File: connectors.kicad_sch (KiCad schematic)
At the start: 9 parts, among them J1 DX07S024JJ2R1300, J2 PCIe_x4_Conn_EdgeMount

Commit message: Updated libraries, finished PCIe clock generator section
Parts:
- C1, C6: footprint antmicro-footprints:0805-cap -> antmicro-footprints:C_0805_2012Metric
- R1: footprint antmicro-footprints:0402-res -> antmicro-footprints:R_0402_1005Metric
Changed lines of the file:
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@@
     (pin "1")
   )
-  (symbol (lib_name "C_10u_0805_35V_1") (lib_id "antmicroCapacitorsmisc:C_10u_0805_35V") (at 181.61 250.19 90) (unit 1)
+  (symbol (lib_id "antmicroCapacitorsmisc:C_10u_0805_35V") (at 181.61 250.19 90) (unit 1)
     (in_bom yes) (on_board yes)
     (property "Reference" "C6" (id 0) (at 183.515 246.38 90)
@@
       (effects (font (size 1.27 1.27) (thickness 0.15)) (justify left bottom) hide)
     )
-    (property "Footprint" "antmicro-footprints:0805-cap" (id 2) (at 194.31 229.87 0)
+    (property "Footprint" "antmicro-footprints:C_0805_2012Metric" (id 2) (at 194.31 229.87 0)
       (effects (font (size 1.27 1.27) (thickness 0.15)) (justify left bottom) hide)
     )
@@
     (pin "1")
   )
-  (symbol (lib_name "C_100n_0402_1") (lib_id "antmicroCapacitors0402:C_100n_0402") (at 140.335 126.365 90) (unit 1)
+  (symbol (lib_id "antmicroCapacitors0402:C_100n_0402") (at 140.335 126.365 90) (unit 1)
     (in_bom yes) (on_board yes)
     (property "Reference" "C2" (id 0) (at 140.97 121.92 90)
@@
     (pin "1")
   )
-  (symbol (lib_name "C_100n_0402_1") (lib_id "antmicroCapacitors0402:C_100n_0402") (at 146.685 126.365 90) (unit 1)
+  (symbol (lib_id "antmicroCapacitors0402:C_100n_0402") (at 146.685 126.365 90) (unit 1)
     (in_bom yes) (on_board yes)
     (property "Reference" "C3" (id 0) (at 147.32 121.92 90)
@@
     (pin "1")
   )
-  (symbol (lib_name "DX07S024JJ2R1300_1") (lib_id "antmicroUSBDVIHDMIConnectors:DX07S024JJ2R1300") (at 138.43 59.69 0) (unit 1)
+  (symbol (lib_id "antmicroUSBDVIHDMIConnectors:DX07S024JJ2R1300") (at 138.43 59.69 0) (unit 1)
     (in_bom yes) (on_board yes) (fields_autoplaced)
     (property "Reference" "J1" (id 0) (at 149.86 46.355 0)
@@
     (pin "1")
   )
-  (symbol (lib_name "C_100n_0402_1") (lib_id "antmicroCapacitors0402:C_100n_0402") (at 159.385 126.365 90) (unit 1)
+  (symbol (lib_id "antmicroCapacitors0402:C_100n_0402") (at 159.385 126.365 90) (unit 1)
     (in_bom yes) (on_board yes)
     (property "Reference" "C5" (id 0) (at 160.02 121.92 90)
@@
     (pin "2")
   )
-  (symbol (lib_name "C_10u_0805_35V_1") (lib_id "antmicroCapacitorsmisc:C_10u_0805_35V") (at 120.65 250.19 90) (unit 1)
+  (symbol (lib_id "antmicroCapacitorsmisc:C_10u_0805_35V") (at 120.65 250.19 90) (unit 1)
     (in_bom yes) (on_board yes)
     (property "Reference" "C1" (id 0) (at 122.555 246.38 90)
@@
       (effects (font (size 1.27 1.27) (thickness 0.15)) (justify left bottom) hide)
     )
-    (property "Footprint" "antmicro-footprints:0805-cap" (id 2) (at 133.35 229.87 0)
+    (property "Footprint" "antmicro-footprints:C_0805_2012Metric" (id 2) (at 133.35 229.87 0)
       (effects (font (size 1.27 1.27) (thickness 0.15)) (justify left bottom) hide)
     )
@@
     (pin "2")
   )
-  (symbol (lib_name "R_3k3_0402_1") (lib_id "antmicroResistors0402:R_3k3_0402") (at 205.74 277.495 90) (unit 1)
+  (symbol (lib_id "antmicroResistors0402:R_3k3_0402") (at 205.74 277.495 90) (unit 1)
     (in_bom yes) (on_board yes) (fields_autoplaced)
     (property "Reference" "R1" (id 0) (at 207.645 273.6849 90)
@@
       (effects (font (size 1.27 1.27) (thickness 0.15)) (justify left bottom) hide)
     )
-    (property "Footprint" "antmicro-footprints:0402-res" (id 2) (at 220.98 257.175 0)
+    (property "Footprint" "antmicro-footprints:R_0402_1005Metric" (id 2) (at 220.98 257.175 0)
       (effects (font (size 1.27 1.27) (thickness 0.15)) (justify left bottom) hide)
     )
@@
     (pin "2")
   )
-  (symbol (lib_name "C_100n_0402_1") (lib_id "antmicroCapacitors0402:C_100n_0402") (at 153.035 126.365 90) (unit 1)
+  (symbol (lib_id "antmicroCapacitors0402:C_100n_0402") (at 153.035 126.365 90) (unit 1)
     (in_bom yes) (on_board yes)
     (property "Reference" "C4" (id 0) (at 153.67 121.92 90)

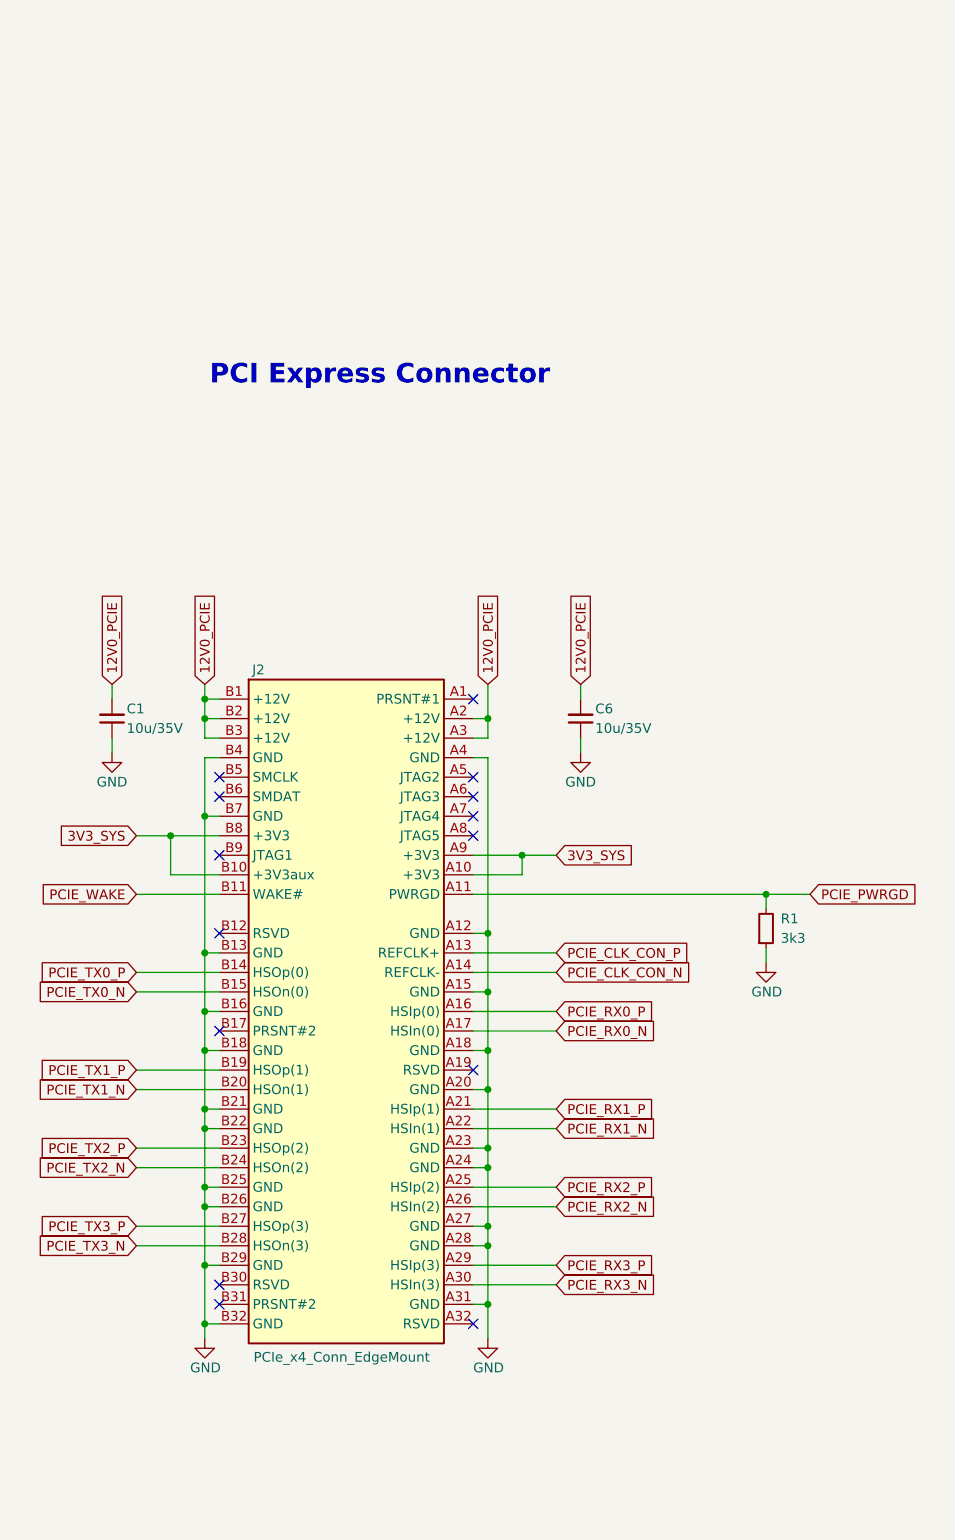
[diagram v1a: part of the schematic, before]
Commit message: Added molex connector and power managment circuity for +12V power rails
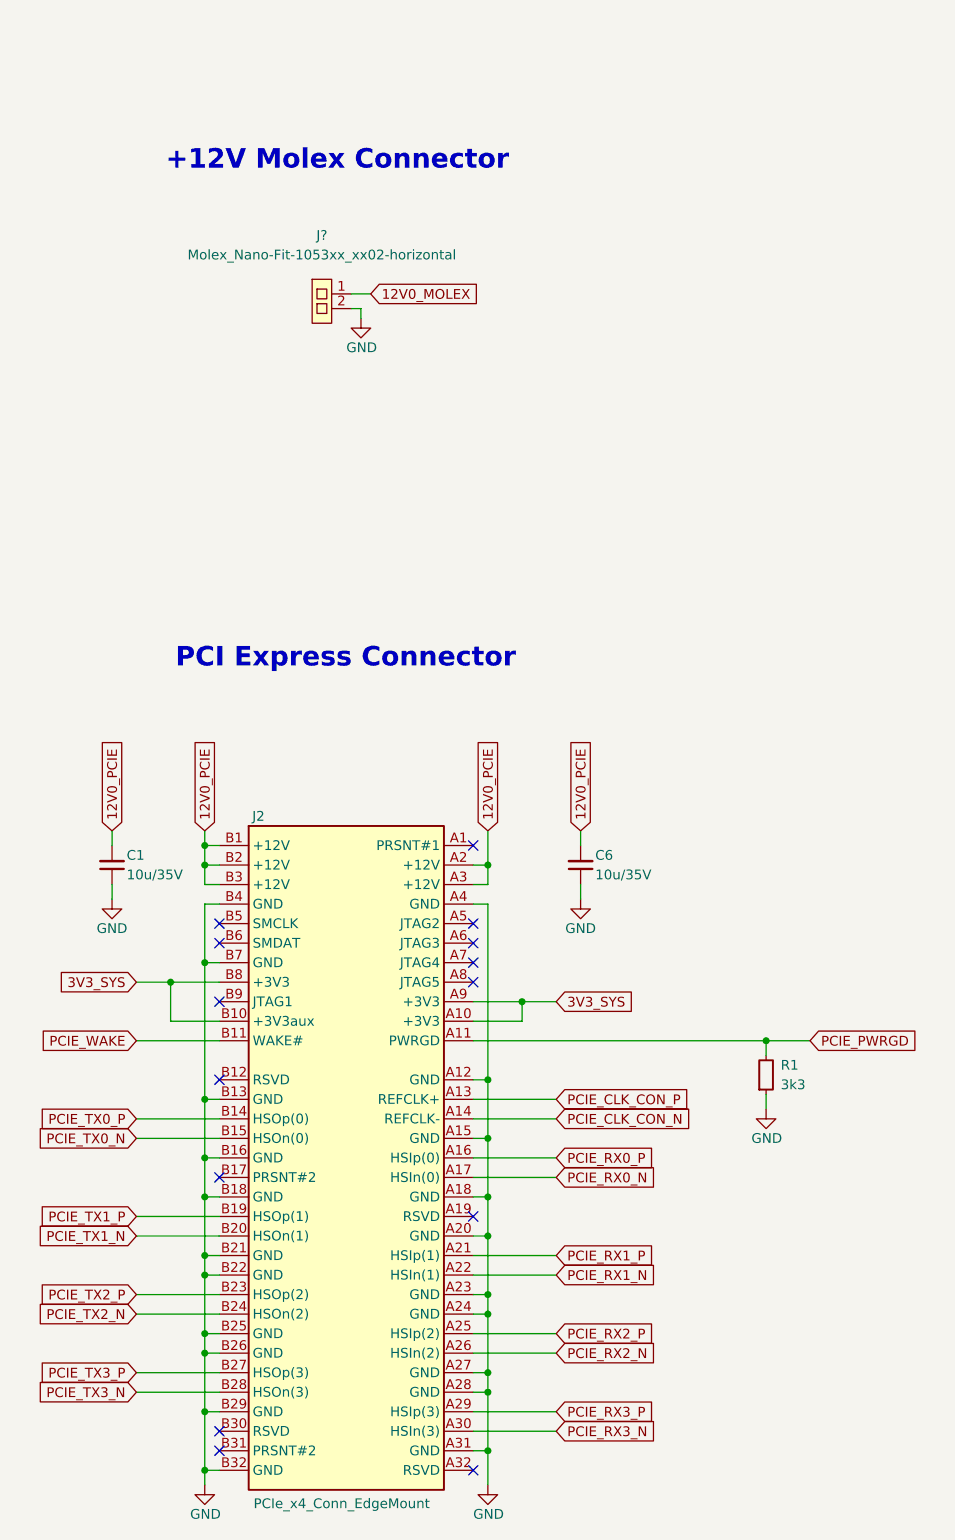
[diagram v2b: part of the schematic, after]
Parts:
- added J?: Molex_Nano-Fit-1053xx_xx02-horizontal, antmicro-footprints:Molex_Nano-Fit_1053xx-xx02_1x02_P2.50mm_Horizontal, symbol antmicroRectangularConnectorsHeadersFemalePins:Molex_Nano-Fit-1053xx_xx02-horiz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
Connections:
- net GND: now also J?.2
- new net 12V0_MOLEX: J?.1
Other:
- note added: "+12V Molex Connector"
- moved on the sheet: C1, C6, J2, R1

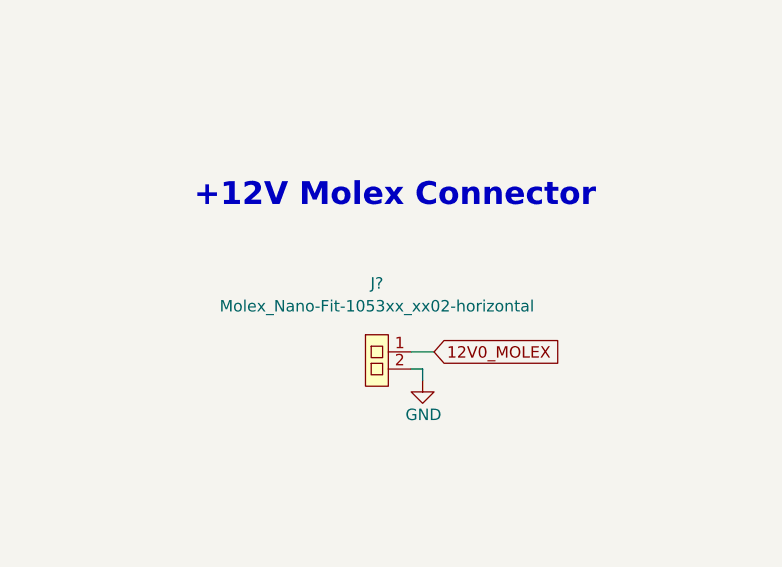
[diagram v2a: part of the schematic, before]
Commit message: Finished placement of molex connector and power management circuity for +12V rails, finished routing of all power planes
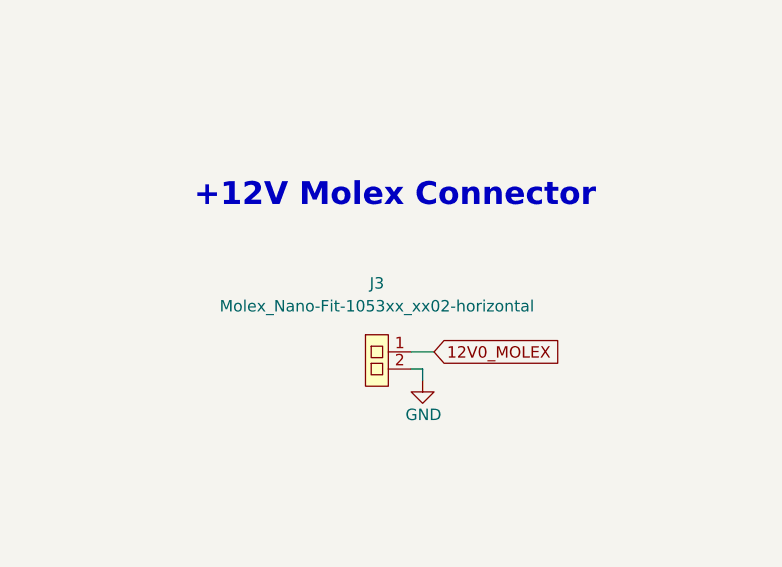
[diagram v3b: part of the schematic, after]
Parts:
- gave numbers to parts that had none: 1
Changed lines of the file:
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@@
   (symbol (lib_id "antmicroRectangularConnectorsHeadersFemalePins:Molex_Nano-Fit-1053xx_xx02-horizontal") (at 146.685 190.5 0) (unit 1)
     (in_bom yes) (on_board yes) (fields_autoplaced)
-    (property "Reference" "J?" (id 0) (at 147.955 184.785 0))
+    (property "Reference" "J3" (id 0) (at 147.955 184.785 0))
     (property "Value" "Molex_Nano-Fit-1053xx_xx02-horizontal" (id 1) (at 147.955 187.325 0))
     (property "Footprint" "antmicro-footprints:Molex_Nano-Fit_1053xx-xx02_1x02_P2.50mm_Horizontal" (id 2) (at 142.24 198.755 0)
@@
   (symbol (lib_id "power:GND") (at 153.035 195.58 0) (unit 1)
     (in_bom yes) (on_board yes)
-    (property "Reference" "#PWR?" (id 0) (at 153.035 201.93 0)
+    (property "Reference" "#PWR0146" (id 0) (at 153.035 201.93 0)
       (effects (font (size 1.27 1.27)) hide)
     )

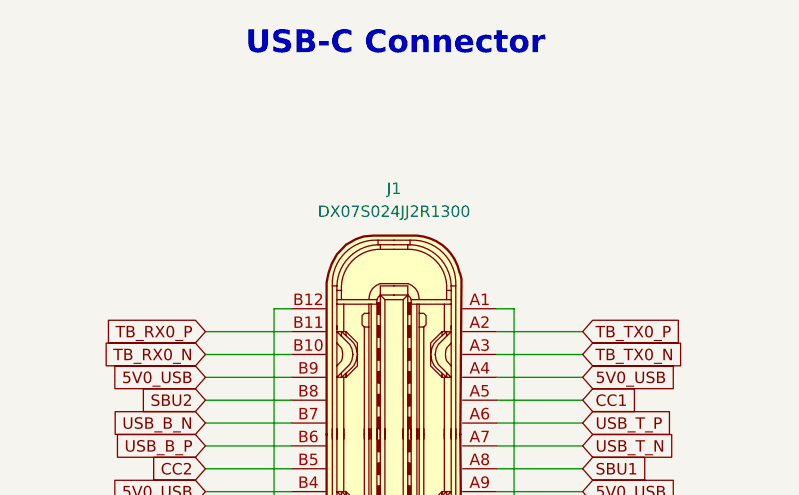
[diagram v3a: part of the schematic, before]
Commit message: Updated symbol and foortpint for USB-C connector to clean related DRC errors
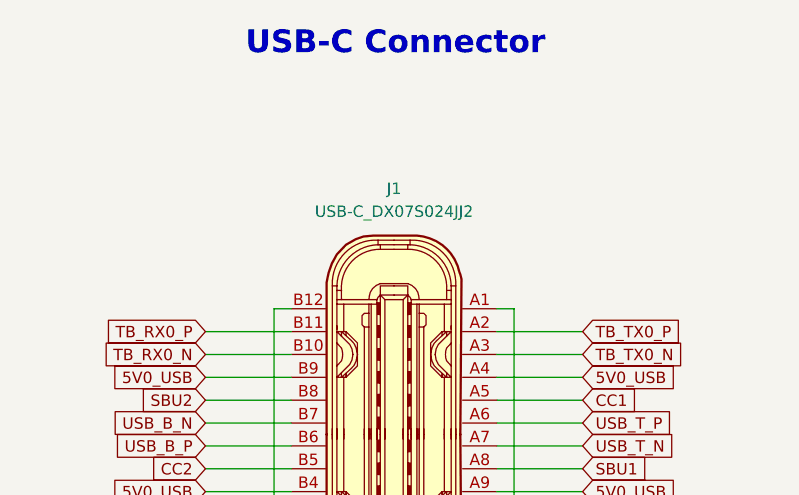
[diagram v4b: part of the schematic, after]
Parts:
- removed J1: DX07S024JJ2R1300, antmicro-footprints:DX07S024JJ2R1300, symbol antmicroUSBDVIHDMIConnectors:DX07S024JJ2R1300
- added J1: USB-C_DX07S024JJ2, antmicro-footprints:USB-3.1-Gen2_Type-C_JAE_DX07S024JJ2_Horizontal, symbol antmicroUSBDVIHDMIConnectors:USB-C_DX07S024JJ2
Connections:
- net 5V0_USB: now also J1.A4, J1.A9, J1.B4, J1.B9
- net CC1: now also J1.A5
- net CC2: now also J1.B5
- net GND: now also J1.A1, J1.A12, J1.B1, J1.B12, J1.SH
- net SBU1: now also J1.A8
- net SBU2: now also J1.B8
- net TB_RX0_N: now also J1.B10
- net TB_RX0_P: now also J1.B11
- net TB_RX1_N: now also J1.A10
- net TB_RX1_P: now also J1.A11
- net TB_TX0_N: now also J1.A3
- net TB_TX0_P: now also J1.A2
- net TB_TX1_N: now also J1.B3
- net TB_TX1_P: now also J1.B2
- net USB_B_N: now also J1.B7
- net USB_B_P: now also J1.B6
- net USB_T_N: now also J1.A7
- net USB_T_P: now also J1.A6
